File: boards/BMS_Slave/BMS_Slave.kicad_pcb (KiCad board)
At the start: 2 copper layers, 155 x 75 mm, 133 parts, among them J1 Mounting_Hole_4-40, J2 Mounting_Hole_4-40, J3 Mounting_Hole_4-40, J4 Mounting_Hole_4-40, J5 MicroFit_11, J6 MicroFit_20, J7 NanoFit_2, J8 NanoFit_2, Q1 Q_NPN_BCE, Q10 NMOS_GSD_30V, Q11 NMOS_GSD_30V, Q2 NMOS_GSD_30V, Q3 NMOS_GSD_30V, Q4 NMOS_GSD_30V, Q5 NMOS_GSD_30V, Q6 NMOS_GSD_30V, Q7 NMOS_GSD_30V, Q8 NMOS_GSD_30V, Q9 NMOS_GSD_30V, T1 T_LAN_7490100111A, U1 LTC6811-1, U2 24AA01, U3 MCP6001, U4 LTC1380, U5 LTC1380, U6 MCP6001

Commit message: Updated PCB Layout 11-4
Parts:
- J5: value MicroFit_11 -> MicroFit_12; footprint footprints:Molex_MicroFit_3.0-11x3.00mm_Angled -> footprints:Microfit3_Header_02x06_Angled_OEM
- moved U5 113.1 mm to (97.8, 77.5)
- moved U4 105.4 mm to (97.8, 69.8)
- moved U6 100.5 mm to (106.7, 76.2)
- moved U3 74.9 mm to (141.0, 118.1)
- moved U2 72.6 mm to (141.0, 114.3)
- moved D10 64.8 mm to (395.6, 165.6)
- moved D6 64.8 mm to (355.4, 165.6)
- moved Q10 64.8 mm to (398.2, 159.6)
- moved Q6 64.8 mm to (358.0, 159.6)
- moved R30 64.8 mm to (365.7, 134.8)
- moved R39 64.8 mm to (366.4, 158.8)
- moved R47 64.8 mm to (406.6, 134.8)
- moved R55 64.8 mm to (406.6, 158.8)
- moved C15 64.8 mm to (369.5, 134.7)
- moved C18 64.8 mm to (365.9, 164.1)
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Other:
- outline, holes or cut-outs redrawn
- board text added: "For Instructional Use Only."
- board text added: "SOLIDWORKS Educational Product."

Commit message: BMS_Slave: first pass layout
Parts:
- moved R57 298.0 mm to (115.6, 85.1), turned to 180 degrees
- moved R55 268.9 mm to (148.6, 83.2), turned to 180 degrees
- moved C22 265.4 mm to (144.8, 91.4), turned to 180 degrees
- moved R58 263.4 mm to (144.8, 86.4)
- moved C20 261.9 mm to (144.8, 123.8), turned to 180 degrees
- moved R50 260.7 mm to (144.8, 97.8)
- moved R47 260.4 mm to (149.2, 95.2), turned to 180 degrees
- moved Q10 259.8 mm to (148.6, 87.6)
- moved D10 256.2 mm to (152.4, 85.1)
- moved R39 255.9 mm to (115.6, 108.0)
- moved Q8 252.3 mm to (148.6, 99.1)
- moved D6 250.4 mm to (111.8, 108.0), turned to 180 degrees
- moved R42 248.4 mm to (120.7, 105.4), turned to 180 degrees
- moved Q6 247.5 mm to (116.8, 104.1), turned to 180 degrees
- moved D8 246.4 mm to (153.7, 95.2)
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
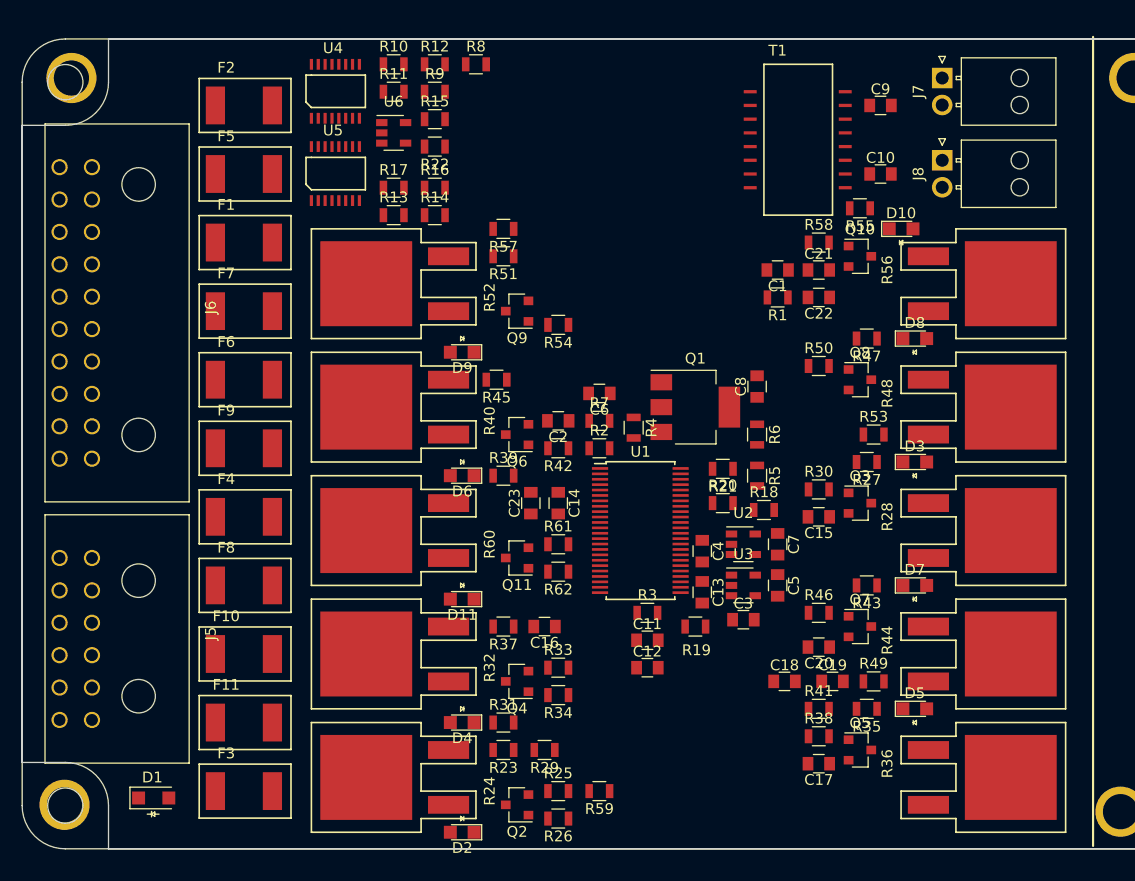
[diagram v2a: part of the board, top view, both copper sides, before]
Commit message: BMS Slave: around 1/2 of layout and tracing done
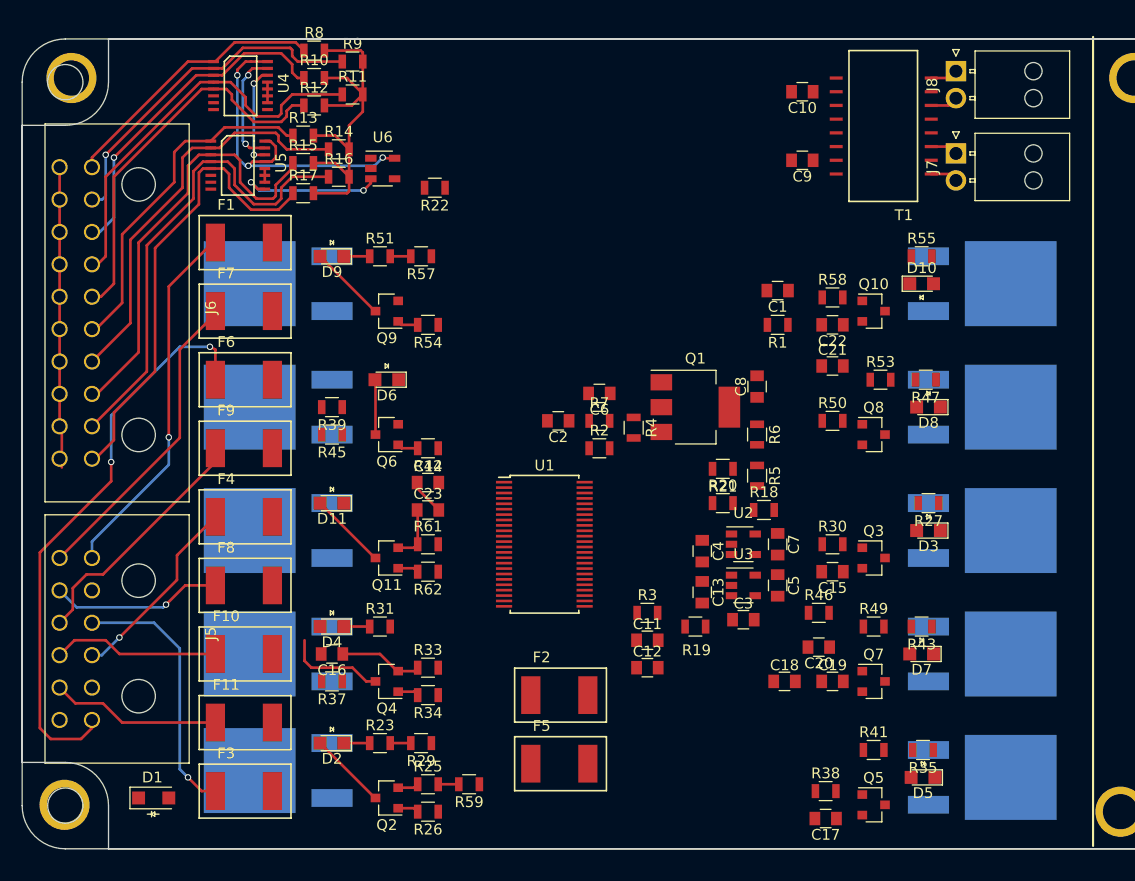
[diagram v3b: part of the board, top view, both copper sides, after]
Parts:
- R24, R28, R32, R36, R40, R44, R48, R52, R56, R60: moved to B.Cu
- moved F2 61.9 mm to (118.1, 128.3)
- moved F5 61.9 mm to (118.1, 134.6)
- moved C16 19.8 mm to (99.7, 124.5)
- moved T1 18.4 mm to (155.2, 80.0), turned to 180 degrees
- moved R39 17.1 mm to (99.7, 101.6), turned to 180 degrees
- moved R37 16.7 mm to (99.7, 127.0)
- moved R45 16.1 mm to (99.7, 104.1)
- moved R8 15.0 mm to (98.0, 68.6)
- moved D11 15.0 mm to (99.7, 110.5)
- moved D4 15.0 mm to (99.7, 121.9)
- moved D9 15.0 mm to (99.7, 87.6)
- moved D2 14.6 mm to (99.7, 132.7)
- moved R31 14.5 mm to (104.1, 121.9)
- moved R15 12.9 mm to (97.0, 79.0)
- moved C14 12.2 mm to (108.6, 108.6), turned to 0 degrees
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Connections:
- J6 pad 4: /CELL_TEMP5 -> /CELL_TEMP4
- J6 pad 5: /CELL_TEMP6 -> /CELL_TEMP5
- T1 pad 1: Net-(J7-Pad1) -> Net-(J7-Pad2)
- T1 pad 3: Net-(J7-Pad2) -> Net-(J7-Pad1)
- T1 pad 6: Net-(J8-Pad1) -> Net-(J8-Pad2)
- T1 pad 8: Net-(J8-Pad2) -> Net-(J8-Pad1)
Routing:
- net Net-(F6-Pad1): track 0.00 -> 53.2 mm, vias 0 -> 2
- net /CELL_TEMP9: track 0.00 -> 44.6 mm
- net /CELL_TEMP10: track 0.00 -> 42.7 mm
- net /CELL_TEMP8: track 0.00 -> 40.3 mm
- net /CELL_TEMP7: track 0.00 -> 37.8 mm
- net /CELL_TEMP4: track 0.00 -> 37.5 mm
- net /VREF2: track 0.00 -> 36.2 mm
- net /CELL_TEMP5: track 0.00 -> 35.9 mm
- net Net-(F1-Pad1): track 0.00 -> 34.1 mm, vias 0 -> 1
- net /CELL_TEMP2: track 0.00 -> 32.1 mm, vias 0 -> 1
- net /CELL_TEMP6: track 0.00 -> 32.0 mm
- net /VREG: track 0.00 -> 31.6 mm, vias 0 -> 3
- net /CELL_TEMP3: track 0.00 -> 31.1 mm, vias 0 -> 1
- net GND: track 0.00 -> 31.1 mm
- net Net-(F7-Pad1): track 0.00 -> 28.8 mm
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
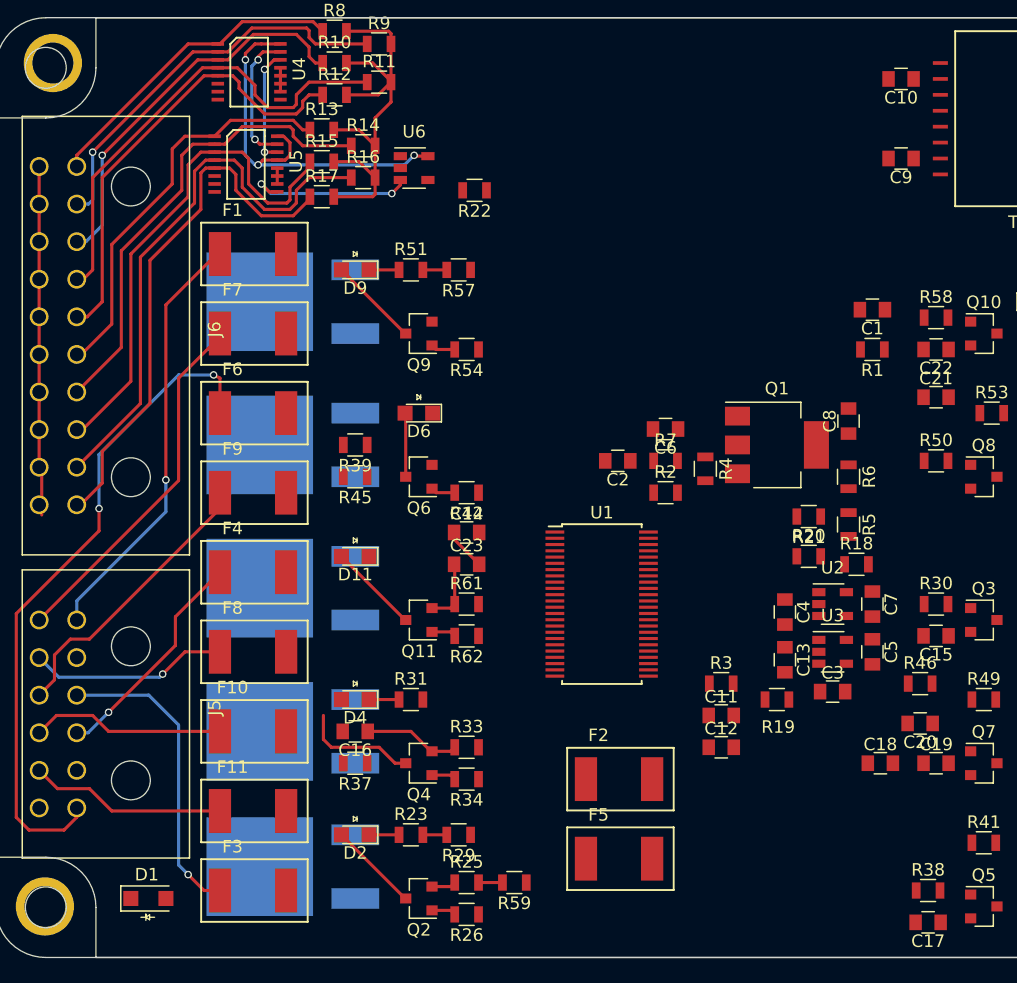
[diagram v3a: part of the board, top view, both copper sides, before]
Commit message: BMS Slave: added inner layers, traced 1/2 of balancers.
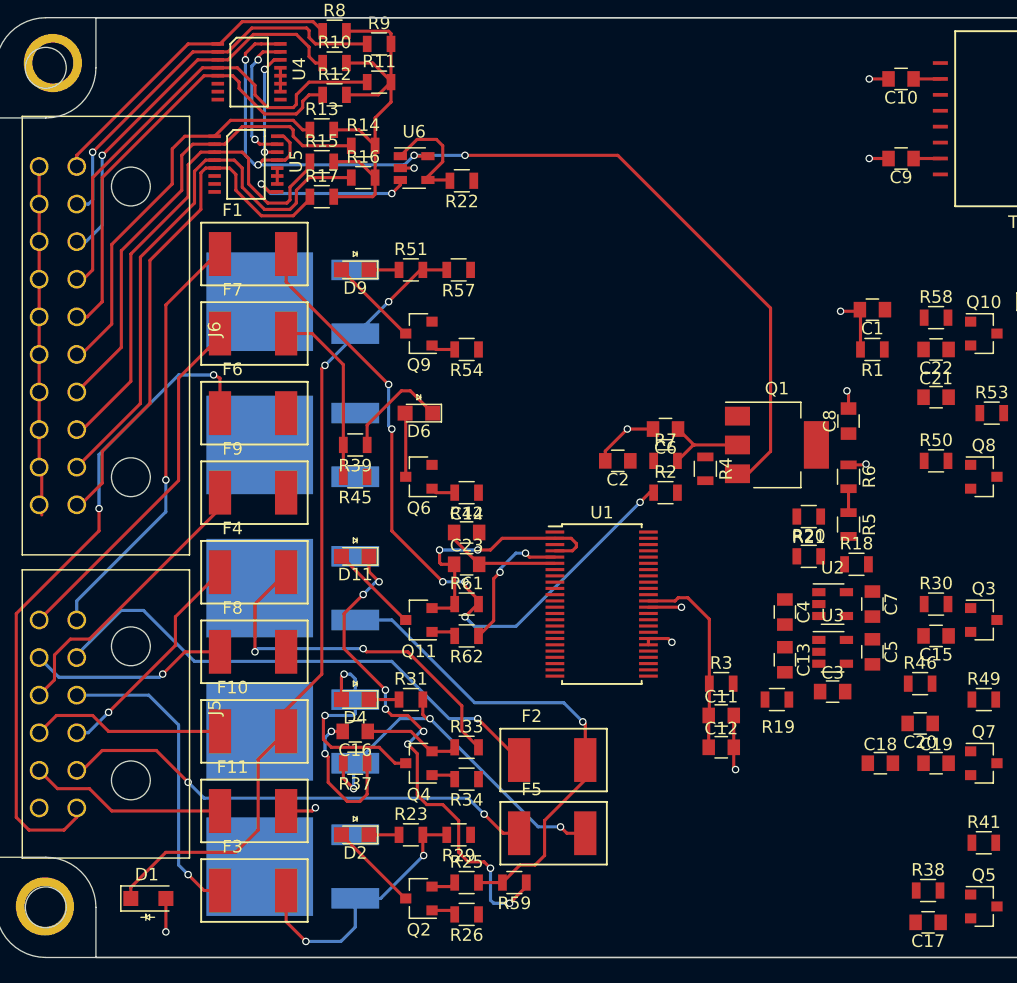
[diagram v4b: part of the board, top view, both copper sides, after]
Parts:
- moved F5 5.71 mm to (112.8, 132.6)
- moved F2 5.55 mm to (112.8, 126.7)
- moved R22 1.27 mm to (108.2, 80.5)
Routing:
- net /VREG: track 31.6 -> 95.8 mm, vias 3 -> 4
- net /Balance2/V_BELOW: track 1.91 -> 65.2 mm, vias 0 -> 2
- net /Balance10/V_CELL: track 0.00 -> 56.6 mm, vias 0 -> 6
- net Net-(F2-Pad1): track 0.00 -> 41.9 mm, vias 0 -> 1
- net Net-(D11-Pad1): track 0.00 -> 41.2 mm, vias 0 -> 8
- net Net-(F5-Pad1): track 0.00 -> 38.7 mm, vias 0 -> 2
- net /Balance10/V_BELOW: track 1.91 -> 39.8 mm, vias 0 -> 1
- net GND: track 31.1 -> 62.9 mm, vias 0 -> 12
- net /Balance7/V_BELOW: track 0.00 -> 30.0 mm, vias 0 -> 3
- net /Balance8/V_BELOW: track 0.00 -> 29.7 mm, vias 0 -> 2
- net /Balance9/V_BELOW: track 1.91 -> 21.9 mm, vias 0 -> 2
- net /Balance10/CELL_SENSE: track 5.14 -> 21.0 mm, vias 0 -> 2
- net /Balance5/V_BELOW: track 0.00 -> 14.5 mm
- net /Balance6/CELL_SENSE: track 0.00 -> 11.7 mm, vias 0 -> 2
- net /Control10: track 0.00 -> 11.1 mm, vias 0 -> 2
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- added copper zone on In1.Cu, net GND
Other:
- copper layers 2 -> 4

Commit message: BMS_Slave: next iteration
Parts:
- F10, F11, F7, F8, F9: moved to B.Cu
- moved C3 173.5 mm to (303.5, 69.9)
- moved J3 166.7 mm to (234.1, 88.9)
- moved C12 163.0 mm to (286.6, 84.4)
- moved R3 162.7 mm to (286.3, 79.1)
- moved C8 161.3 mm to (298.5, 75.4), turned to 0 degrees
- moved J1 160.9 mm to (234.1, 98.6)
- moved C5 158.2 mm to (294.2, 79.0), turned to 0 degrees
- moved R20 157.6 mm to (290.4, 79.1)
- moved R19 154.8 mm to (282.1, 79.1), turned to 0 degrees
- moved C13 152.5 mm to (282.6, 84.4), turned to 0 degrees
- moved R4 151.4 mm to (278.3, 88.2), turned to 0 degrees
- moved C1 149.8 mm to (290.6, 84.4), turned to 0 degrees
- moved C7 143.7 mm to (282.6, 89.7), turned to 0 degrees
- moved R18 138.2 mm to (276.8, 93.6)
- moved R5 134.7 mm to (273.0, 93.6), turned to 0 degrees
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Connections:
- J5 pad 10: Net-(F10-Pad1) -> Net-(F8-Pad1)
- J5 pad 2: Net-(F2-Pad1) -> Net-(F3-Pad1)
- J5 pad 3: Net-(F3-Pad1) -> Net-(F5-Pad1)
- J5 pad 4: Net-(F4-Pad1) -> Net-(F7-Pad1)
- J5 pad 5: Net-(F5-Pad1) -> Net-(F9-Pad1)
- J5 pad 6: Net-(F6-Pad1) -> Net-(F10-Pad1)
- J5 pad 7: Net-(F7-Pad1) -> Net-(F2-Pad1)
- J5 pad 8: Net-(F8-Pad1) -> Net-(F4-Pad1)
- J5 pad 9: Net-(F9-Pad1) -> Net-(F6-Pad1)
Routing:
- net /Balance2/V_BELOW: track 65.2 -> 0.00 mm, vias 2 -> 0
- net /VREG: track 95.8 -> 31.6 mm, vias 4 -> 3
- net /Balance10/V_CELL: track 56.6 -> 0.00 mm, vias 6 -> 0
- net Net-(F6-Pad1): track 53.2 -> 0.00 mm, vias 2 -> 0
- net Net-(F2-Pad1): track 41.9 -> 0.00 mm, vias 1 -> 0
- net Net-(D11-Pad1): track 41.2 -> 0.00 mm, vias 8 -> 0
- net /Balance10/V_BELOW: track 39.8 -> 0.00 mm, vias 1 -> 0
- net Net-(F5-Pad1): track 38.7 -> 0.00 mm, vias 2 -> 0
- net Net-(F1-Pad1): track 34.1 -> 0.00 mm, vias 1 -> 0
- net /Balance7/V_BELOW: track 30.0 -> 0.00 mm, vias 3 -> 0
- net /Balance8/V_BELOW: track 29.7 -> 0.00 mm, vias 2 -> 0
- net Net-(F7-Pad1): track 28.8 -> 0.00 mm
- net GND: track 62.9 -> 35.3 mm, vias 12 -> 3
- net Net-(F3-Pad1): track 24.4 -> 0.21 mm, vias 1 -> 0
- net Net-(F9-Pad1): track 23.0 -> 0.45 mm
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
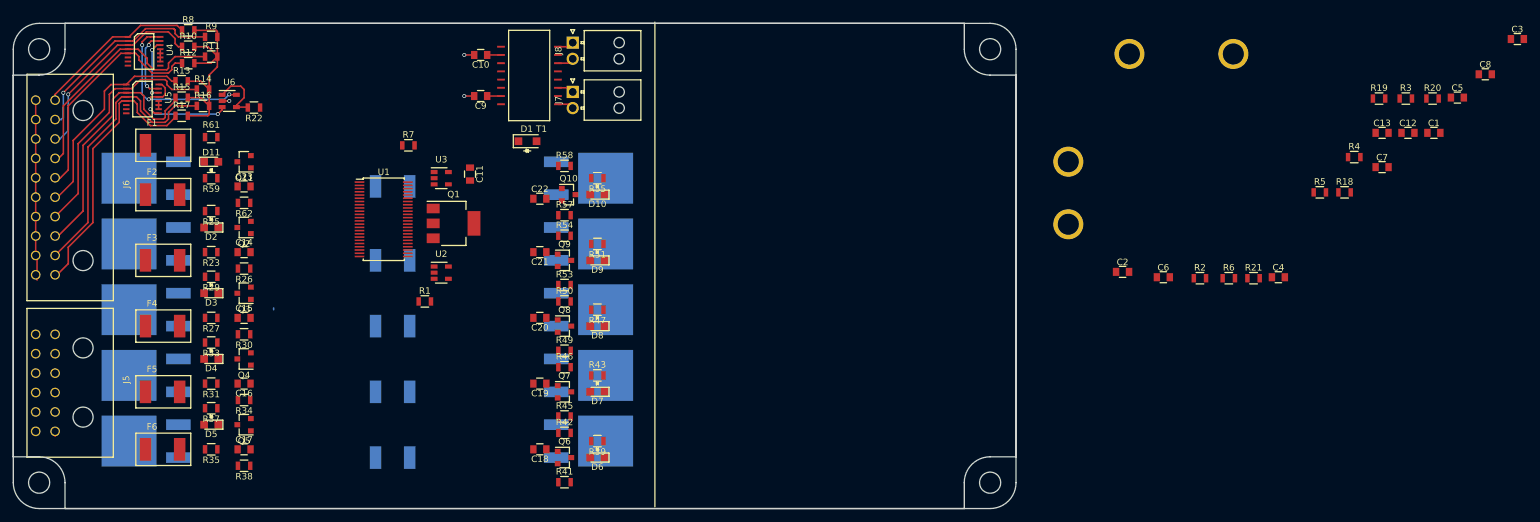
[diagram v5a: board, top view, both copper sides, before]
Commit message: BMS Slave: began tracing.
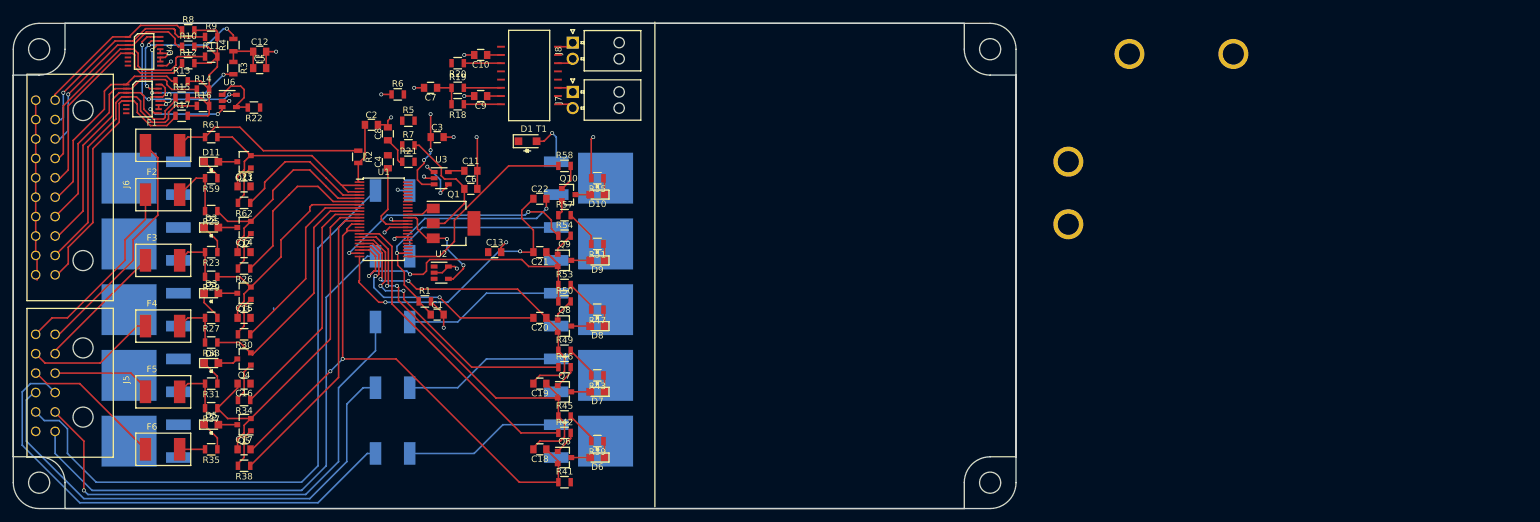
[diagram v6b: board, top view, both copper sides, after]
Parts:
- moved C5 185.2 mm to (109.1, 74.4)
- moved R3 181.3 mm to (105.0, 74.4), turned to 270 degrees
- moved C12 177.9 mm to (109.1, 71.9)
- moved R4 174.1 mm to (105.0, 70.9), turned to 90 degrees
- moved C8 169.9 mm to (128.9, 84.6), turned to 90 degrees
- moved C3 167.7 mm to (136.5, 85.1)
- moved C1 156.6 mm to (136.5, 112.5)
- moved R20 150.8 mm to (139.7, 73.7), turned to 180 degrees
- moved C7 147.6 mm to (135.5, 77.5), turned to 180 degrees
- moved R19 142.4 mm to (139.7, 77.5)
- moved R5 141.3 mm to (132.1, 82.5)
- moved C4 138.8 mm to (128.9, 88.9), turned to 90 degrees
- moved C13 138.4 mm to (145.4, 102.9)
- moved R18 137.8 mm to (139.7, 80.0), turned to 180 degrees
- moved R21 131.9 mm to (132.1, 88.9)
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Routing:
- net Net-(F11-Pad1): track 0.00 -> 97.6 mm
- net /Balance5/CELL_SENSE: track 0.00 -> 91.8 mm, vias 0 -> 2
- net Net-(F10-Pad1): track 0.75 -> 85.6 mm
- net Net-(F9-Pad1): track 0.45 -> 78.8 mm, vias 0 -> 1
- net Net-(F8-Pad1): track 0.00 -> 78.2 mm
- net Net-(F7-Pad1): track 0.00 -> 75.9 mm
- net /Balance4/CELL_SENSE: track 0.00 -> 60.9 mm, vias 0 -> 2
- net GND: track 35.3 -> 93.8 mm, vias 3 -> 20
- net /Balance6/CELL_SENSE: track 0.00 -> 56.3 mm
- net /Balance3/CELL_SENSE: track 0.00 -> 51.6 mm, vias 0 -> 2
- net /Control5: track 0.00 -> 48.7 mm
- net /Balance1/CELL_SENSE: track 0.00 -> 47.8 mm, vias 0 -> 2
- net /Balance2/CELL_SENSE: track 0.00 -> 46.7 mm, vias 0 -> 2
- net /Control6: track 0.00 -> 46.1 mm
- net /Control4: track 0.00 -> 43.7 mm, vias 0 -> 2
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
